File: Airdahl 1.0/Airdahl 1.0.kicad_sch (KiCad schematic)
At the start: 29 parts, among them J1 Conn_ARM_JTAG_SWD_20, SW1 SW_MEC_5E, U1 STM32F446RETx, X2 ABS25-32.768KHZ-6-T, Y1 ABM3B-8.000MHZ-12-D1X-T

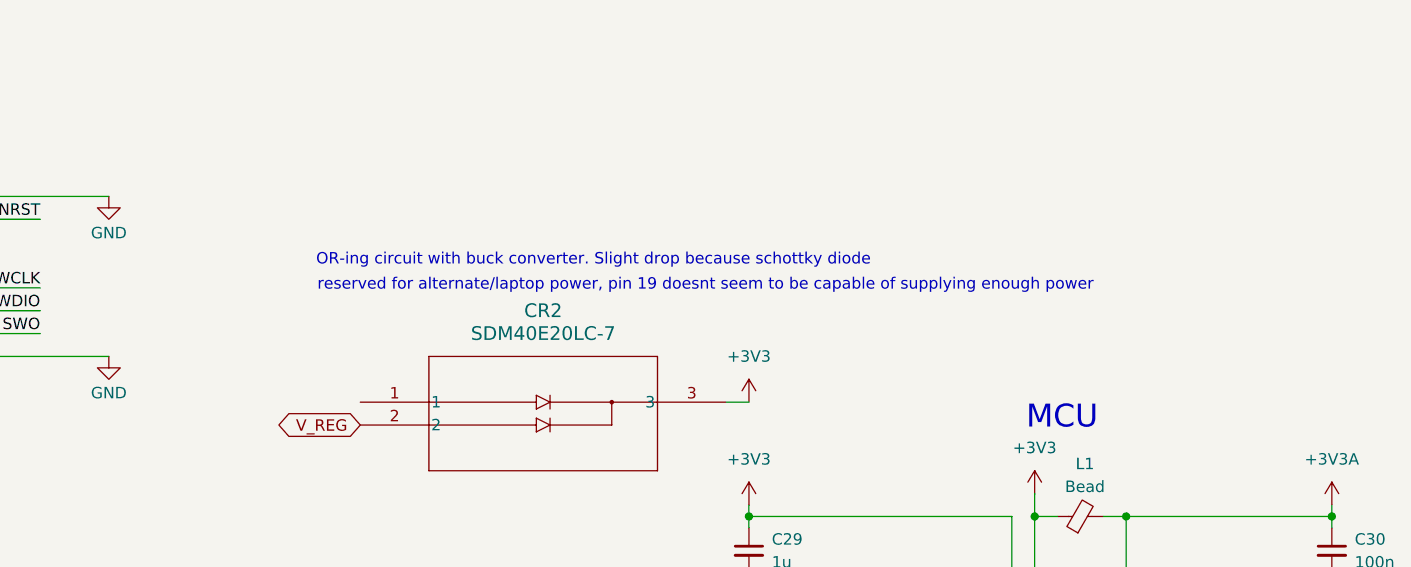
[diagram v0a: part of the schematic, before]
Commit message: reworked pyro circuit for higher current, split off pyro 3.3v into its own rail, some schematic cleanup
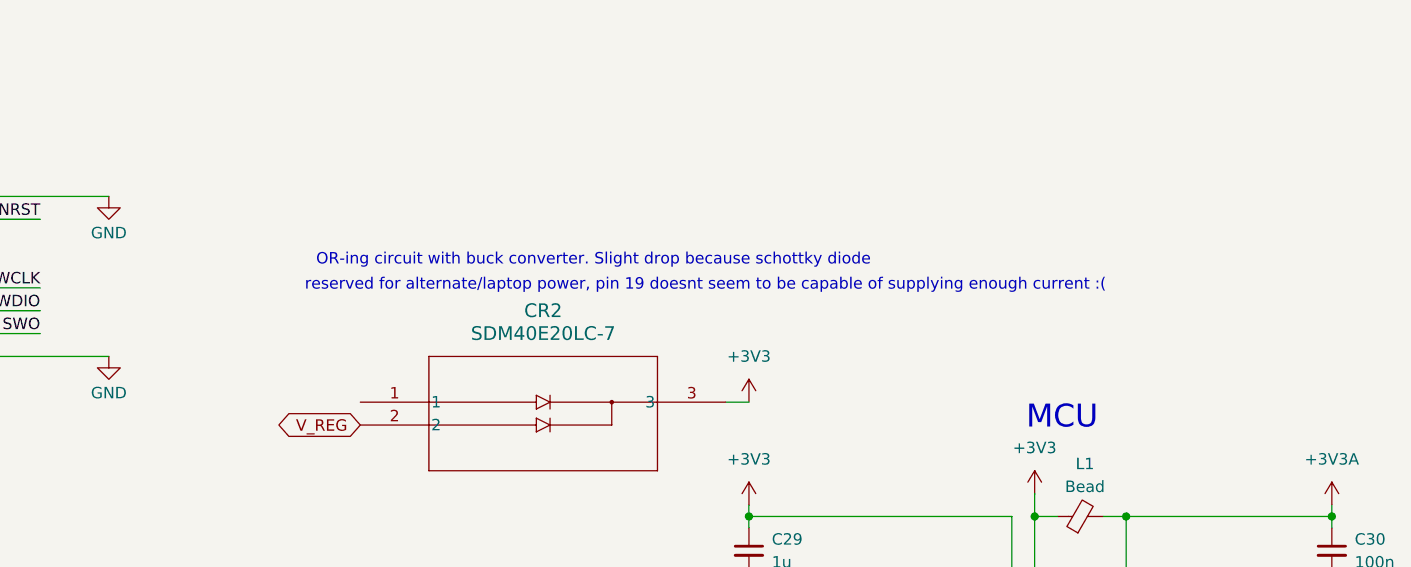
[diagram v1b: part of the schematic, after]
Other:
- note added: "reserved for alternate/laptop power, pin 19 doesnt seem to be capable of supplying enough current :("
- note removed: "reserved for alternate/laptop power, pin 19 doesnt seem to be capable of supplying enough power"
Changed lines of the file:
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@@
 		(rev "1")
 	)
-	(text "reserved for alternate/laptop power, pin 19 doesnt seem to be capable of supplying enough power"
+	(text "reserved for alternate/laptop power, pin 19 doesnt seem to be capable of supplying enough current :("
 		(exclude_from_sim no)
 		(at 156.464 50.546 0)
